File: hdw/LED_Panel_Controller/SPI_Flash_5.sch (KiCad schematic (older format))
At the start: 14 parts

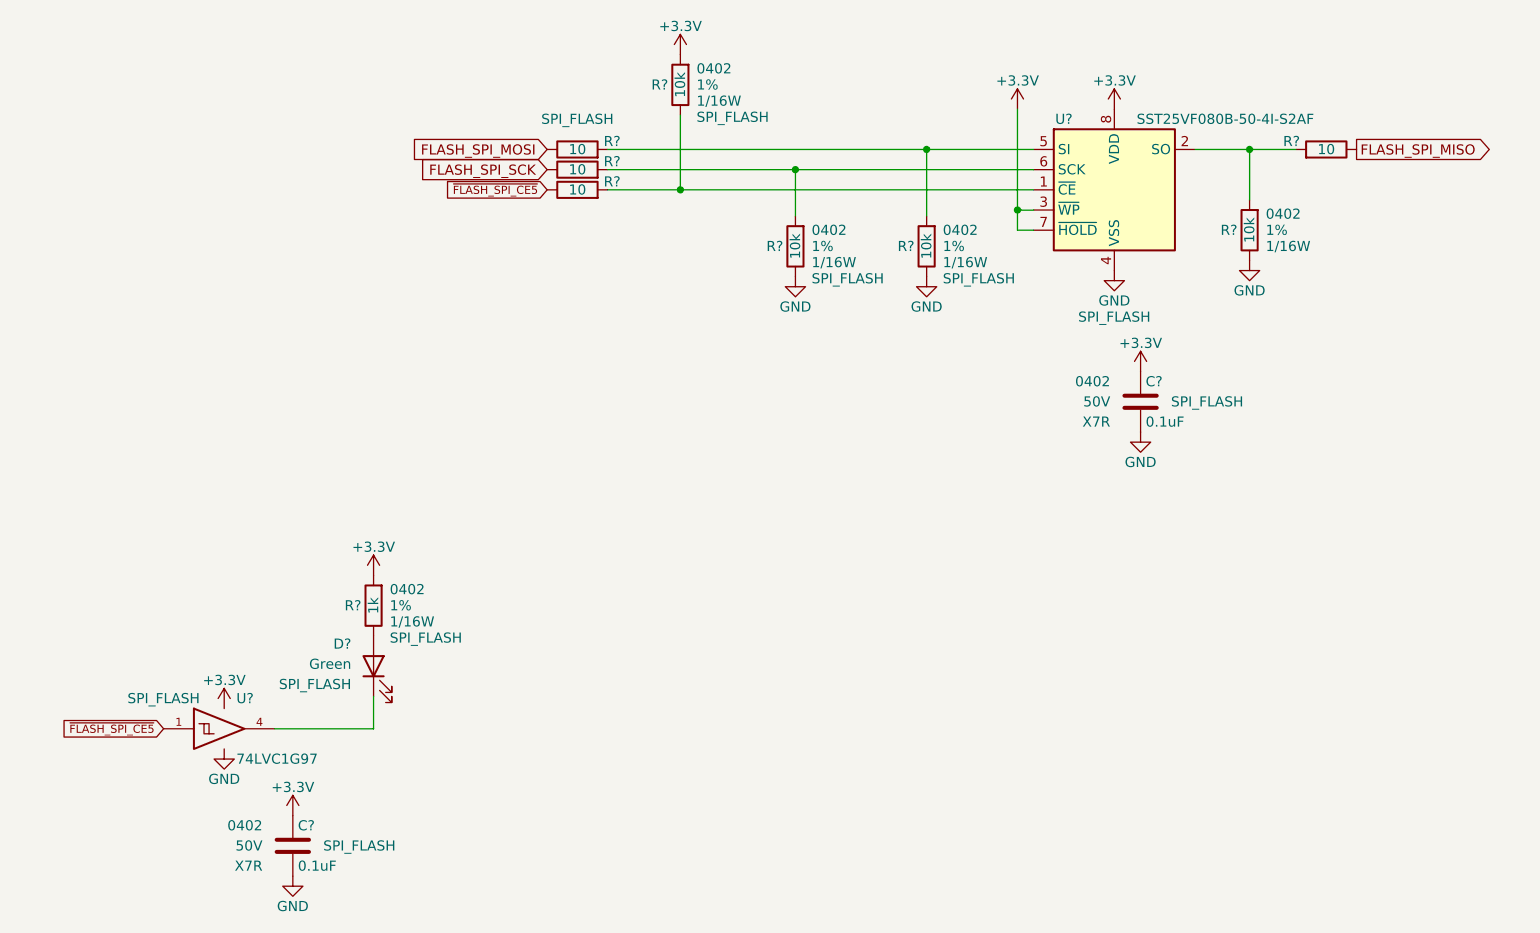
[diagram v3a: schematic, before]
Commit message: assigned I2C addresses
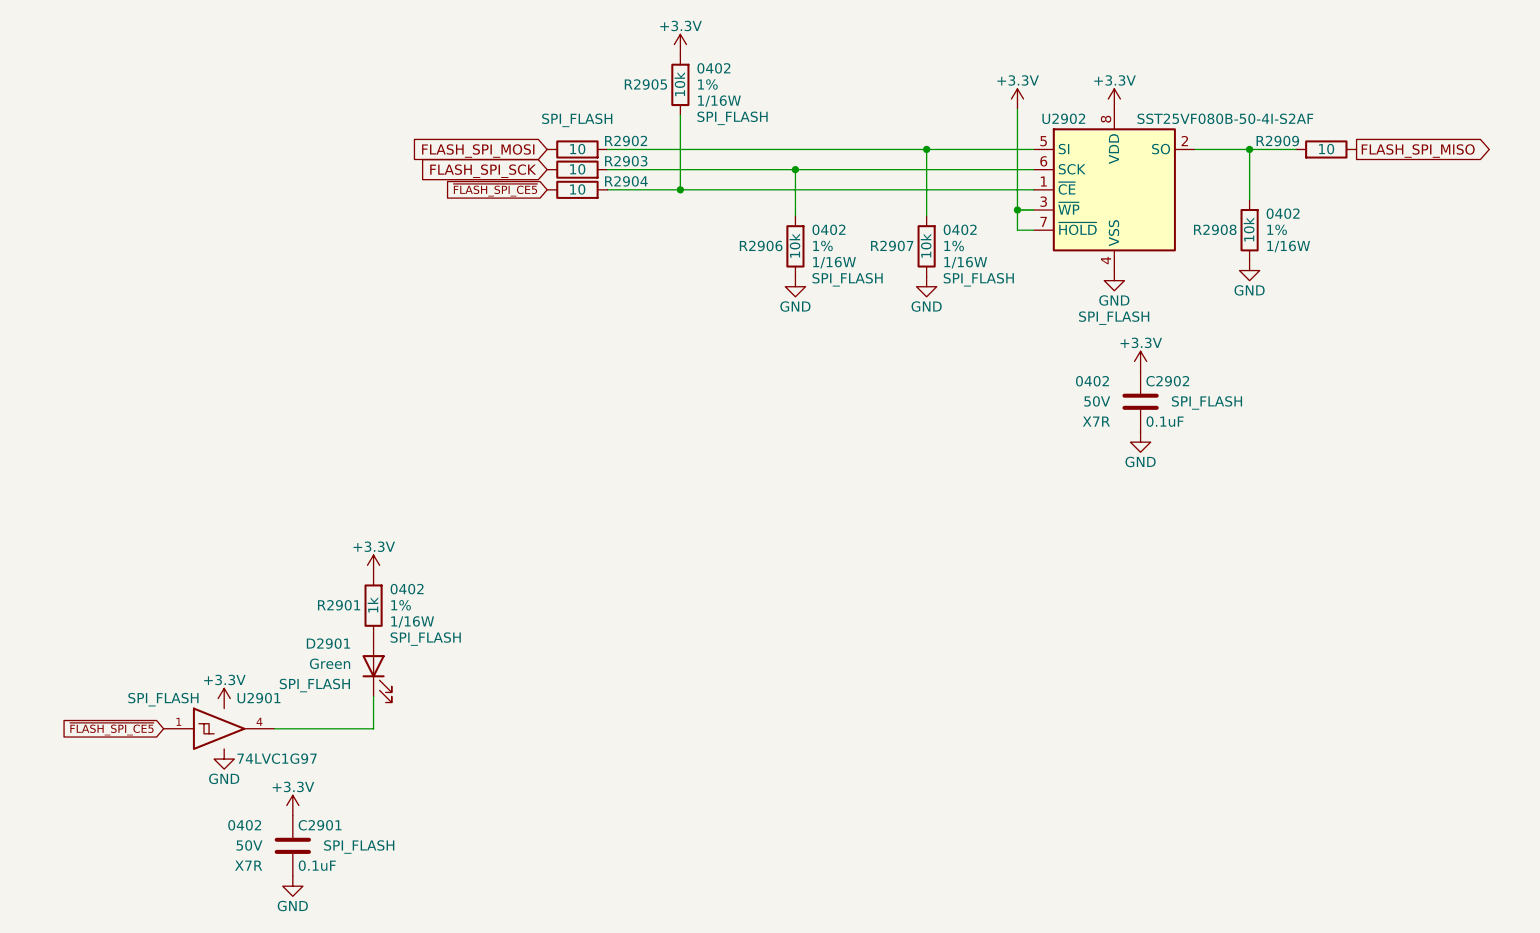
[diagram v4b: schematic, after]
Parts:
- removed C?: 0.1uF, Capacitors_SMD:C_0402, symbol Custom_Library:C_Custom
- removed D?: Green, LEDs:LED_0402, symbol Device:LED
- removed R? (x4): 10k, Resistors_SMD:R_0402, symbol Custom_Library:R_Custom
- removed R? (x4): 10, Resistors_SMD:R_0402, symbol Custom_Library:R_Custom
- removed R?: 1k, Resistors_SMD:R_0402, symbol Custom_Library:R_Custom
- removed U?: SST25VF080B-50-4I-S2AF, Package_SO:SOIC-8_5.275x5.275mm_P1.27mm, symbol Memory_Flash:SST25VF080B-50-4x-S2Ax
- removed U?: 74LVC1G97, Package_TO_SOT_SMD:SOT-363_SC-70-6, symbol Custom_Library:74LVC1G97_Power_BUF
- added C2901: 0.1uF, Capacitors_SMD:C_0402, symbol Custom_Library:C_Custom
- added D2901: Green, LEDs:LED_0402, symbol Device:LED
- added R2901: 1k, Resistors_SMD:R_0402, symbol Custom_Library:R_Custom
- added R2902, R2903, R2904, R2909: 10, Resistors_SMD:R_0402, symbol Custom_Library:R_Custom
- added R2905, R2906, R2907, R2908: 10k, Resistors_SMD:R_0402, symbol Custom_Library:R_Custom
- added U2901: 74LVC1G97, Package_TO_SOT_SMD:SOT-363_SC-70-6, symbol Custom_Library:74LVC1G97_Power_BUF
- added U2902: SST25VF080B-50-4I-S2AF, Package_SO:SOIC-8_5.275x5.275mm_P1.27mm, symbol Memory_Flash:SST25VF080B-50-4x-S2Ax
- gave numbers to parts that had none: 1
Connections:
- net +3V3: now also C2901.1, R2901.1, R2905.1, U2901.5 (VCC), U2902.3 (~WP~), U2902.7 (~HOLD~), U2902.8 (VDD)
- net FLASH_SPI_MISO: now also R2909.2
- net FLASH_SPI_MOSI: now also R2902.2
- net FLASH_SPI_SCK: now also R2903.2
- net GND: now also C2901.2, R2906.2, R2907.2, R2908.2, U2901.2 (GND), U2901.3 (GND), U2901.6 (GND), U2902.4 (VSS)
- net ~FLASH_SPI_CE5: now also R2904.2, U2901.1
- new net: R2908.1, R2909.1, U2902.2 (SO)
- new net: R2902.1, R2907.1, U2902.5 (SI)
- new net: D2901.1 (K), U2901.4
- new net: D2901.2 (A), R2901.2
- new net: R2904.1, R2905.2, U2902.1 (~CE)
- new net: R2903.1, R2906.1, U2902.6 (SCK)
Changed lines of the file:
@@
 $EndDescr
 $Comp
-L power:GND #PWR?
-U 1 1 5BB4E0E3
+L power:GND #PWR02911
+U 1 1 6078625D
 P 6080 4050
-F 0 "#PWR?" H 6080 3800 50  0001 C CNN
+F 0 "#PWR02911" H 6080 3800 50  0001 C CNN
 F 1 "GND" H 6080 3900 50  0000 C CNN
 F 2 "" H 6080 4050 50  0001 C CNN
@@
 $EndComp
 $Comp
-L Custom_Library:R_Custom R?
-U 1 1 5BB4EDD1
+L Custom_Library:R_Custom R2908
+U 1 1 60786266
 P 6750 3850
-F 0 "R?" H 6690 3850 50  0000 R CNN
+F 0 "R2908" H 6690 3850 50  0000 R CNN
 F 1 "10k" V 6750 3850 50  0000 C CNN
 F 2 "Resistors_SMD:R_0402" H 6750 3850 50  0001 C CNN
@@
 $EndComp
 $Comp
-L power:GND #PWR?
-U 1 1 5BB4EE63
+L power:GND #PWR02908
+U 1 1 60786271
 P 5150 4080
-F 0 "#PWR?" H 5150 3830 50  0001 C CNN
+F 0 "#PWR02908" H 5150 3830 50  0001 C CNN
 F 1 "GND" H 5150 3930 50  0000 C CNN
 F 2 "" H 5150 4080 50  0001 C CNN
@@
 $EndComp
 $Comp
-L power:GND #PWR?
-U 1 1 5BB4EE7C
+L power:GND #PWR02914
+U 1 1 60786276
 P 6750 4000
-F 0 "#PWR?" H 6750 3750 50  0001 C CNN
+F 0 "#PWR02914" H 6750 3750 50  0001 C CNN
 F 1 "GND" H 6750 3850 50  0000 C CNN
 F 2 "" H 6750 4000 50  0001 C CNN
@@
 $EndComp
 $Comp
-L Custom_Library:R_Custom R?
-U 1 1 5BB4F53B
+L Custom_Library:R_Custom R2902
+U 1 1 6078627A
 P 3420 3450
-F 0 "R?" V 3380 3580 50  0000 L CNN
+F 0 "R2902" V 3380 3580 50  0000 L CNN
 F 1 "10" V 3420 3450 50  0000 C CNN
 F 2 "Resistors_SMD:R_0402" H 3420 3450 50  0001 C CNN
@@
 	3570 3650 3930 3650
 $Comp
-L power:+3.3V #PWR?
-U 1 1 5BDF3D33
+L power:+3.3V #PWR02906
+U 1 1 60786283
 P 3930 2980
-F 0 "#PWR?" H 3930 2830 50  0001 C CNN
+F 0 "#PWR02906" H 3930 2830 50  0001 C CNN
 F 1 "+3.3V" H 3930 3120 50  0000 C CNN
 F 2 "" H 3930 2980 50  0001 C CNN
@@
 $EndComp
 $Comp
-L power:+3.3V #PWR?
-U 1 1 5BDF3DF4
+L power:+3.3V #PWR02910
+U 1 1 60786288
 P 6080 3250
-F 0 "#PWR?" H 6080 3100 50  0001 C CNN
+F 0 "#PWR02910" H 6080 3100 50  0001 C CNN
 F 1 "+3.3V" H 6080 3390 50  0000 C CNN
 F 2 "" H 6080 3250 50  0001 C CNN
@@
 $Comp
 L Custom_Library:C_Custom C?
-U 1 1 5C15F697
+U 1 1 60786293
 P 2010 6900
-AR Path="/5BAAE16C/5C15F697" Ref="C?"  Part="1"
-AR Path="/5BB181D8/5C15F697" Ref="C?"  Part="1"
-AR Path="/5BB2595E/5C15F697" Ref="C?"  Part="1"
-AR Path="/5F583577/5C15F697" Ref="C?"  Part="1"
-AR Path="/5F5835A4/5C15F697" Ref="C?"  Part="1"
-F 0 "C?" H 2035 7000 50  0000 L CNN
+AR Path="/5BAAE16C/60786293" Ref="C?"  Part="1"
+AR Path="/5BB181D8/60786293" Ref="C?"  Part="1"
+AR Path="/5BB2595E/60786293" Ref="C?"  Part="1"
+AR Path="/5F583577/60786293" Ref="C?"  Part="1"
+AR Path="/5F5835A4/60786293" Ref="C2901"  Part="1"
+F 0 "C2901" H 2035 7000 50  0000 L CNN
 F 1 "0.1uF" H 2035 6800 50  0000 L CNN
 F 2 "Capacitors_SMD:C_0402" H 2048 6750 50  0001 C CNN
@@
 $EndComp
 $Comp
-L power:+3.3V #PWR?
-U 1 1 5C161B83
+L power:+3.3V #PWR02901
+U 1 1 60786297
 P 1670 6220
-F 0 "#PWR?" H 1670 6070 50  0001 C CNN
+F 0 "#PWR02901" H 1670 6070 50  0001 C CNN
 F 1 "+3.3V" H 1670 6360 50  0000 C CNN
 F 2 "" H 1670 6220 50  0001 C CNN
@@
 $EndComp
 $Comp
-L power:+3.3V #PWR?
-U 1 1 5C161BE9
+L power:+3.3V #PWR02903
+U 1 1 607862A0
 P 2010 6750
-F 0 "#PWR?" H 2010 6600 50  0001 C CNN
+F 0 "#PWR02903" H 2010 6600 50  0001 C CNN
 F 1 "+3.3V" H 2010 6890 50  0000 C CNN
 F 2 "" H 2010 6750 50  0001 C CNN
@@
 $EndComp
 $Comp
-L power:GND #PWR?
-U 1 1 5C161C44
+L power:GND #PWR02904
+U 1 1 607862A3
 P 2010 7050
-F 0 "#PWR?" H 2010 6800 50  0001 C CNN
+F 0 "#PWR02904" H 2010 6800 50  0001 C CNN
 F 1 "GND" H 2010 6900 50  0000 C CNN
 F 2 "" H 2010 7050 50  0001 C CNN
@@
 $EndComp
 $Comp
-L power:GND #PWR?
-U 1 1 5C161C9F
+L power:GND #PWR02902
+U 1 1 607862AA
 P 1670 6420
-F 0 "#PWR?" H 1670 6170 50  0001 C CNN
+F 0 "#PWR02902" H 1670 6170 50  0001 C CNN
 F 1 "GND" H 1670 6270 50  0000 C CNN
 F 2 "" H 1670 6420 50  0001 C CNN
@@
 $Comp
 L power:+3.3V #PWR?
-U 1 1 5C166A81
+U 1 1 607862B3
 P 2410 5560
-AR Path="/5BB844FD/5C166A81" Ref="#PWR?"  Part="1"
-AR Path="/5BF346B3/5C166A81" Ref="#PWR?"  Part="1"
-AR Path="/5BB2595E/5C166A81" Ref="#PWR?"  Part="1"
-AR Path="/5F583577/5C166A81" Ref="#PWR?"  Part="1"
-AR Path="/5F5835A4/5C166A81" Ref="#PWR?"  Part="1"
-F 0 "#PWR?" H 2410 5410 50  0001 C CNN
+AR Path="/5BB844FD/607862B3" Ref="#PWR?"  Part="1"
+AR Path="/5BF346B3/607862B3" Ref="#PWR?"  Part="1"
+AR Path="/5BB2595E/607862B3" Ref="#PWR?"  Part="1"
+AR Path="/5F583577/607862B3" Ref="#PWR?"  Part="1"
+AR Path="/5F5835A4/607862B3" Ref="#PWR02905"  Part="1"
+F 0 "#PWR02905" H 2410 5410 50  0001 C CNN
 F 1 "+3.3V" H 2410 5700 50  0000 C CNN
 F 2 "" H 2410 5560 50  0001 C CNN
@@
 $Comp
 L Device:LED D?
-U 1 1 5C166A95
+U 1 1 607862BD
 P 2410 6010
-AR Path="/5BB844FD/5C166A95" Ref="D?"  Part="1"
-AR Path="/5BF346B3/5C166A95" Ref="D?"  Part="1"
-AR Path="/5BB2595E/5C166A95" Ref="D?"  Part="1"
-AR Path="/5F583577/5C166A95" Ref="D?"  Part="1"
-AR Path="/5F5835A4/5C166A95" Ref="D?"  Part="1"
-F 0 "D?" V 2520 6120 50  0000 L CNN
+AR Path="/5BB844FD/607862BD" Ref="D?"  Part="1"
+AR Path="/5BF346B3/607862BD" Ref="D?"  Part="1"
+AR Path="/5BB2595E/607862BD" Ref="D?"  Part="1"
+AR Path="/5F583577/607862BD" Ref="D?"  Part="1"
+AR Path="/5F5835A4/607862BD" Ref="D2901"  Part="1"
+F 0 "D2901" V 2520 6120 50  0000 L CNN
 F 1 "Green" V 2420 6120 50  0000 L CNN
 F 2 "LEDs:LED_0402" H 2410 6010 50  0001 C CNN
@@
 $EndComp
 $Comp
-L Memory_Flash:SST25VF080B-50-4x-S2Ax U?
-U 1 1 5F6879D5
+L Memory_Flash:SST25VF080B-50-4x-S2Ax U2902
+U 1 1 607862F6
 P 6080 3650
-F 0 "U?" H 5830 4000 50  0000 C CNN
+F 0 "U2902" H 5830 4000 50  0000 C CNN
 F 1 "SST25VF080B-50-4I-S2AF" H 6630 4000 50  0000 C CNN
 F 2 "Package_SO:SOIC-8_5.275x5.275mm_P1.27mm" H 6080 2950 50  0001 C CNN
@@
 $EndComp
 $Comp
-L power:+3.3V #PWR?
-U 1 1 5F689292
+L power:+3.3V #PWR02912
+U 1 1 60786302
 P 6210 4550
-F 0 "#PWR?" H 6210 4400 50  0001 C CNN
+F 0 "#PWR02912" H 6210 4400 50  0001 C CNN
 F 1 "+3.3V" H 6210 4690 50  0000 C CNN
 F 2 "" H 6210 4550 50  0001 C CNN
@@
 $EndComp
 $Comp
-L power:GND #PWR?
-U 1 1 5F689298
+L power:GND #PWR02913
+U 1 1 60786307
 P 6210 4850
-F 0 "#PWR?" H 6210 4600 50  0001 C CNN
+F 0 "#PWR02913" H 6210 4600 50  0001 C CNN
 F 1 "GND" H 6210 4700 50  0000 C CNN
 F 2 "" H 6210 4850 50  0001 C CNN
@@
 $EndComp
 $Comp
-L power:+3.3V #PWR?
+L power:+3.3V #PWR02909
 U 1 1 5F69329F
 P 5600 3250
-F 0 "#PWR?" H 5600 3100 50  0001 C CNN
+F 0 "#PWR02909" H 5600 3100 50  0001 C CNN
 F 1 "+3.3V" H 5600 3390 50  0000 C CNN
 F 2 "" H 5600 3250 50  0001 C CNN
@@
 	3570 3550 4500 3550
 $Comp
-L Custom_Library:R_Custom R?
-U 1 1 5F697048
+L Custom_Library:R_Custom R2906
+U 1 1 60786316
 P 4500 3930
-F 0 "R?" H 4440 3930 50  0000 R CNN
+F 0 "R2906" H 4440 3930 50  0000 R CNN
 F 1 "10k" V 4500 3930 50  0000 C CNN
 F 2 "Resistors_SMD:R_0402" H 4500 3930 50  0001 C CNN
@@
 $EndComp
 $Comp
-L power:GND #PWR?
+L power:GND #PWR02907
 U 1 1 5F697052
 P 4500 4080
-F 0 "#PWR?" H 4500 3830 50  0001 C CNN
+F 0 "#PWR02907" H 4500 3830 50  0001 C CNN
 F 1 "GND" H 4500 3930 50  0000 C CNN
 F 2 "" H 4500 4080 50  0001 C CNN
@@
 	4500 3550 5680 3550
 $Comp
-L Custom_Library:R_Custom R?
-U 1 1 5F7379BB
+L Custom_Library:R_Custom R2903
+U 1 1 60786324
 P 3420 3550
-F 0 "R?" V 3380 3680 50  0000 L CNN
+F 0 "R2903" V 3380 3680 50  0000 L CNN
 F 1 "10" V 3420 3550 50  0000 C CNN
 F 2 "Resistors_SMD:R_0402" H 3420 3550 50  0001 C CNN
@@
 $EndComp
 $Comp
-L Custom_Library:R_Custom R?
-U 1 1 5F737B74
+L Custom_Library:R_Custom R2904
+U 1 1 6078632C
 P 3420 3650
-F 0 "R?" V 3380 3780 50  0000 L CNN
+F 0 "R2904" V 3380 3780 50  0000 L CNN
 F 1 "10" V 3420 3650 50  0000 C CNN
 F 2 "Resistors_SMD:R_0402" H 3420 3650 50  0001 C CNN
@@
 $EndComp
 $Comp
-L Custom_Library:R_Custom R?
-U 1 1 5F737D15
+L Custom_Library:R_Custom R2909
+U 1 1 60786332
 P 7130 3450
-F 0 "R?" V 7090 3580 50  0000 L CNN
+F 0 "R2909" V 7090 3580 50  0000 L CNN
 F 1 "10" V 7130 3450 50  0000 C CNN
 F 2 "Resistors_SMD:R_0402" H 7130 3450 50  0001 C CNN
@@
 $EndComp
 $Comp
-L Custom_Library:74LVC1G97_Power_BUF U?
-U 1 1 5FE9D8D5
+L Custom_Library:74LVC1G97_Power_BUF U2901
+U 1 1 60786342
 P 1670 6320
-F 0 "U?" H 1730 6470 50  0000 L CNN
+F 0 "U2901" H 1730 6470 50  0000 L CNN
 F 1 "74LVC1G97" H 1730 6170 50  0000 L CNN
 F 2 "Package_TO_SOT_SMD:SOT-363_SC-70-6" H 1720 6320 50  0001 C CNN
@@
 $EndComp
 $Comp
-L Custom_Library:R_Custom R?
-U 1 1 6026393A
+L Custom_Library:R_Custom R2907
+U 1 1 60786356
 P 5150 3930
-F 0 "R?" H 5090 3930 50  0000 R CNN
+F 0 "R2907" H 5090 3930 50  0000 R CNN
 F 1 "10k" V 5150 3930 50  0000 C CNN
 F 2 "Resistors_SMD:R_0402" H 5150 3930 50  0001 C CNN
@@
 $EndComp
 $Comp
-L Custom_Library:R_Custom R?
-U 1 1 60263FB7
+L Custom_Library:R_Custom R2905
+U 1 1 60786361
 P 3930 3130
-F 0 "R?" H 3870 3130 50  0000 R CNN
+F 0 "R2905" H 3870 3130 50  0000 R CNN
 F 1 "10k" V 3930 3130 50  0000 C CNN
 F 2 "Resistors_SMD:R_0402" H 3930 3130 50  0001 C CNN
@@
 $EndComp
 $Comp
-L Custom_Library:R_Custom R?
-U 1 1 60266213
+L Custom_Library:R_Custom R2901
+U 1 1 60786364
 P 2410 5710
-F 0 "R?" H 2350 5710 50  0000 R CNN
+F 0 "R2901" H 2350 5710 50  0000 R CNN
 F 1 "1k" V 2410 5710 50  0000 C CNN
 F 2 "Resistors_SMD:R_0402" H 2410 5710 50  0001 C CNN
@@
 AR Path="/5BB2595E/60269564" Ref="C?"  Part="1"
 AR Path="/5F583577/60269564" Ref="C?"  Part="1"
-AR Path="/5F5835A4/60269564" Ref="C?"  Part="1"
-F 0 "C?" H 6235 4800 50  0000 L CNN
+AR Path="/5F5835A4/60269564" Ref="C2902"  Part="1"
+F 0 "C2902" H 6235 4800 50  0000 L CNN
 F 1 "0.1uF" H 6235 4600 50  0000 L CNN
 F 2 "Capacitors_SMD:C_0402" H 6248 4550 50  0001 C CNN
